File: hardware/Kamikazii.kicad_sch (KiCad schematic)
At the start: 36 parts, among them U1 L7805CV, U2 BP

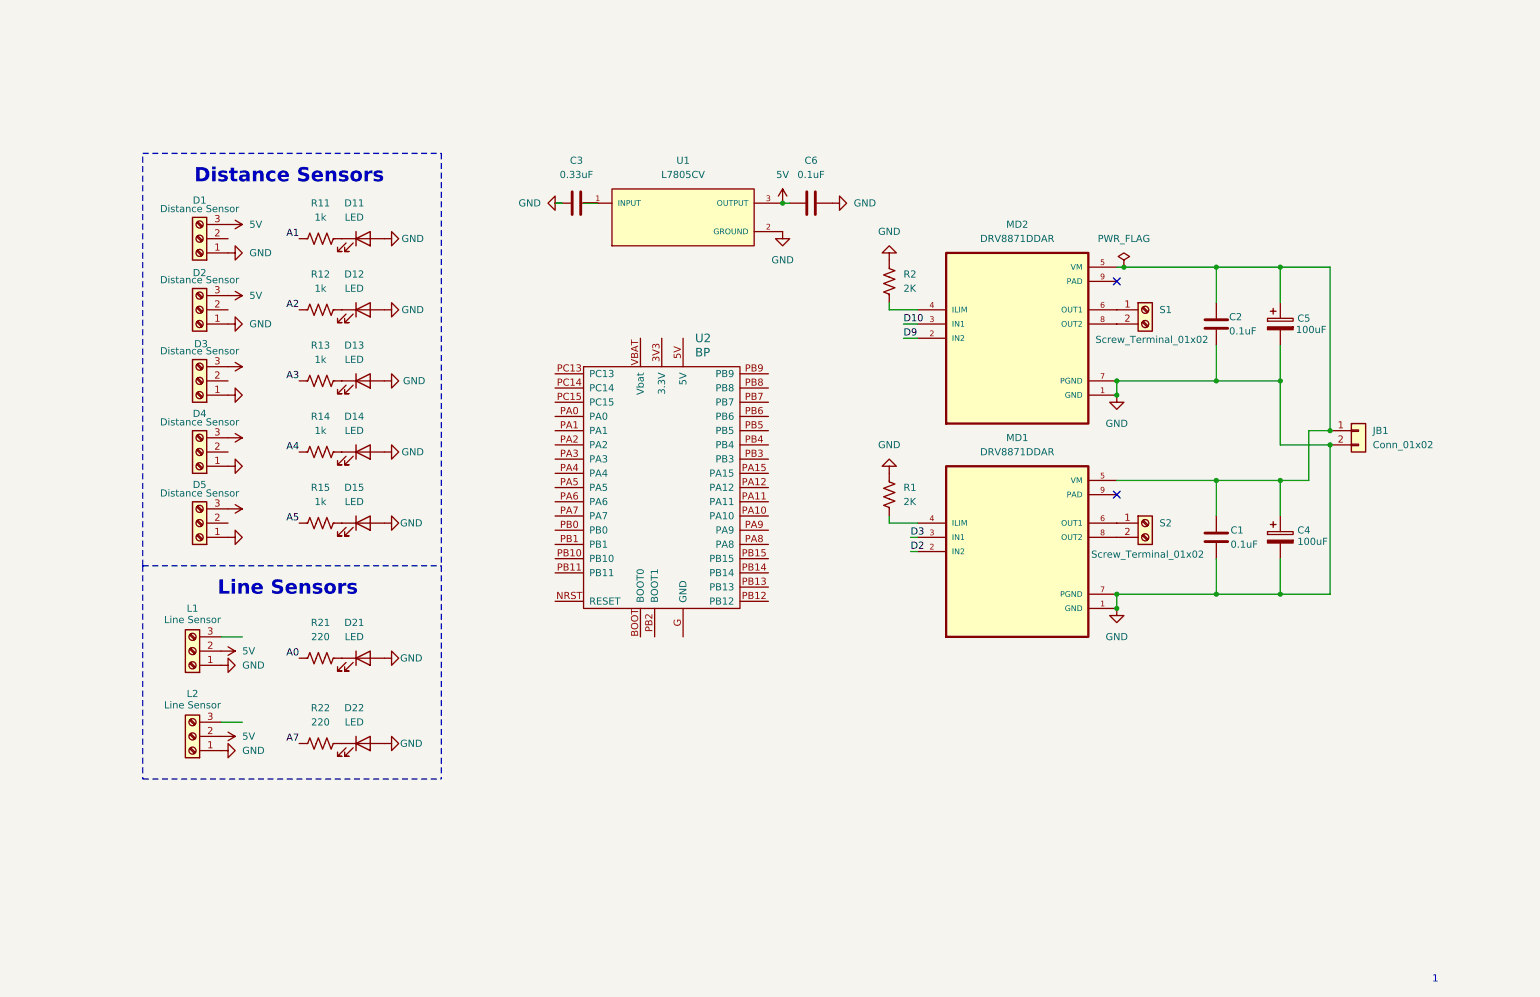
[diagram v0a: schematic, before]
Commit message: Add libraries for components
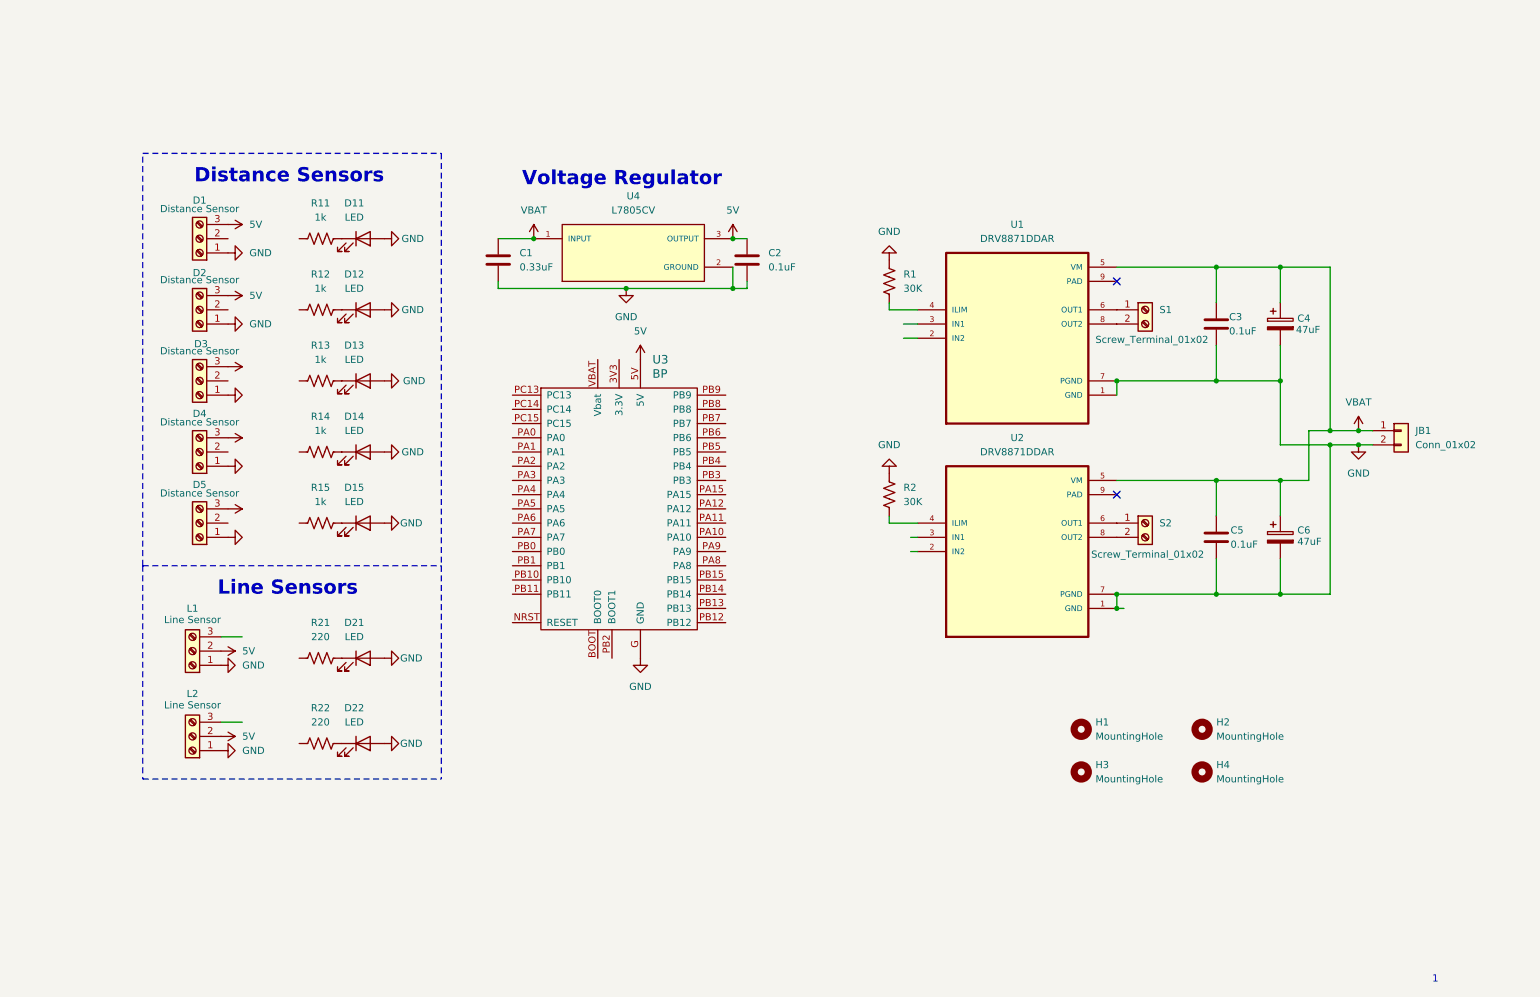
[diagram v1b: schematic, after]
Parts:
- removed MD1, MD2: DRV8871DDAR, DRV8871DDAR:VREG_LM5017MR_NOPB, symbol DRV8871DDAR:DRV8871DDAR
- removed U1: L7805CV, L7805CV:TO255P1040X460X1968-3, symbol L7805CV:L7805CV
- removed U2: BP, blue_pill:blue_pill, symbol STM32DB:BP
- added H1, H2, H3, H4: MountingHole, MountingHole:MountingHole_3.2mm_M3, symbol Mechanical:MountingHole
- added U1, U2: DRV8871DDAR, DRV8871DDAR:VREG_LM5017MR_NOPB, symbol DRV8871DDAR:DRV8871DDAR
- added U3: BP, blue_pill:blue_pill, symbol bp:BP
- added U4: L7805CV, L7805CV:TO255P1040X460X1968-3, symbol L7805CV:L7805CV
- C4: renamed from C5; value 100uF -> 47uF
- C6: renamed from C4; value 100uF -> 47uF
- R1: renamed from R2; value 2K -> 30K
- R2: renamed from R1; value 2K -> 30K
- renumbered C3 to C1, C6 to C2, C2 to C3, C1 to C5
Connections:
- net 5V: now also C2.2, U3.5V, U4.3 (OUTPUT); no longer C2.1
- net GND: now also C2.1, U1.1 (GND), U1.7 (PGND), U2.1 (GND), U2.7 (PGND), U3.G (GND), U4.2 (GROUND); no longer C2.2
- net VBAT: now reaches C3.1, C4.1, C5.1, C6.1, JB1.1 (Pin_1)
- net VBAT: now also C1.2, U1.5 (VM), U2.5 (VM), U4.1 (INPUT)
- net at S1.1 (Pin_1): now also U1.6 (OUT1)
- net at S1.2 (Pin_2): now also U1.8 (OUT2)
- net at R2.2: now also U2.4 (ILIM)
- net at S2.1 (Pin_1): now also U2.6 (OUT1)
- net at S2.2 (Pin_2): now also U2.8 (OUT2)
- net at R1.2: now also U1.4 (ILIM)
- net A0: no longer names the net of R21.1
- net A1: no longer names the net of R11.1
- net A2: no longer names the net of R12.1
- net A3: no longer names the net of R13.1
- net A4: no longer names the net of R14.1
- net A5: no longer names the net of R15.1
- net A7: no longer names the net of R22.1
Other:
- note added: "Voltage Regulator"
- moved on the sheet: C1, C2, JB1

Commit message: Finish schematic
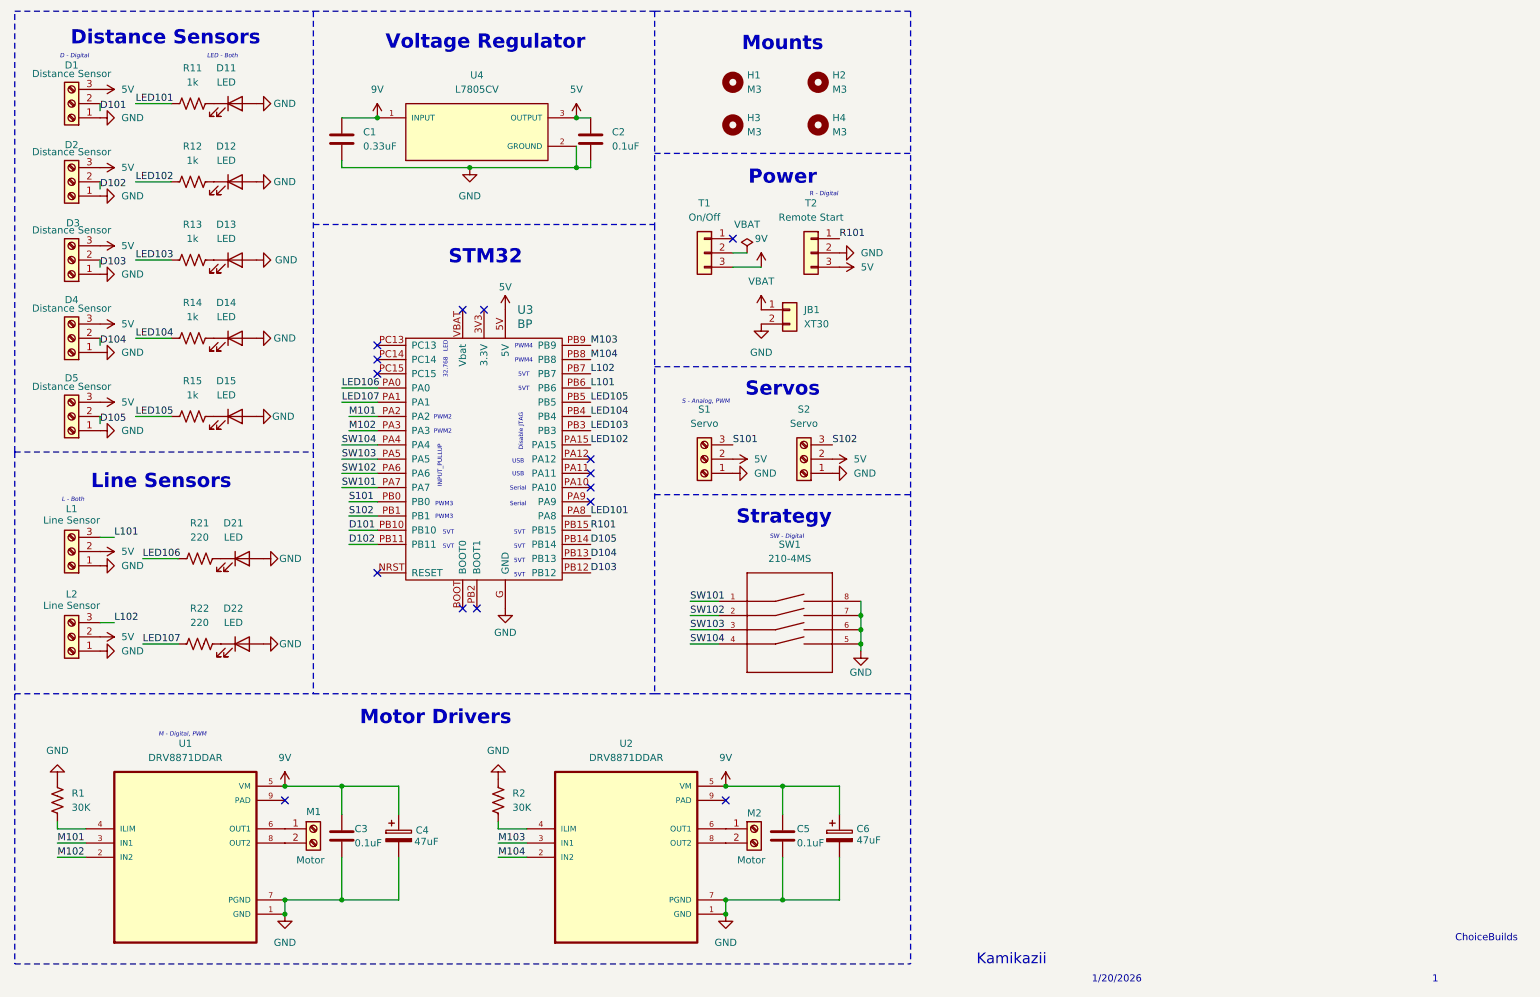
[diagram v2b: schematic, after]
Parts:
- added S1, S2: Servo, TerminalBlock:TerminalBlock_Xinya_XY308-2.54-2P_1x02_P2.54mm_Horizontal, symbol Connector:Screw_Terminal_01x03
- added SW1: 210-4MS, 210-4MS:DIP8_210-4_CTS, symbol 210-4MS:210-4MS
- added T1: On/Off, symbol Connector_Generic:Conn_01x03
- added T2: Remote Start, symbol Connector_Generic:Conn_01x03
- H1, H2, H3, H4: value MountingHole -> M3
- JB1: value Conn_01x02 -> XT30
- M1: renamed from S1; value Screw_Terminal_01x02 -> Motor
- M2: renamed from S2; value Screw_Terminal_01x02 -> Motor
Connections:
- net 5V: now also S1.2 (Pin_2), S2.2 (Pin_2), T2.3 (Pin_3)
- net GND: now also S1.1 (Pin_1), S2.1 (Pin_1), SW1.5, SW1.6, SW1.7, SW1.8, T2.2 (Pin_2)
- net VBAT: no longer C1.2, C3.1, C4.1, C5.1, C6.1, U1.5 (VM), U2.5 (VM), U4.1 (INPUT)
- net D102: now reaches D2.2 (Pin_2)
- net D102: now also U3.PB11
- net LED105: now reaches R15.1
- net LED105: now also U3.PB5
- net LED104: now reaches R14.1
- net LED104: now also U3.PB4
- net D101: now reaches D1.2 (Pin_2)
- net D101: now also U3.PB10
- net LED102: now reaches R12.1
- net LED102: now also U3.PA15
- net D105: now reaches D5.2 (Pin_2)
- net D105: now also U3.PB14
- net M104: now reaches U2.2 (IN2)
- net M104: now also U3.PB8
- net M103: now reaches U2.3 (IN1)
- net M103: now also U3.PB9
- net LED103: now reaches R13.1
- net LED103: now also U3.PB3
- net L101: now reaches L1.3 (Pin_3)
- net L101: now also U3.PB6
- net D103: now reaches D3.2 (Pin_2)
- net D103: now also U3.PB12
- net LED107: now reaches R22.1
- net LED107: now also U3.PA1
- net LED106: now reaches R21.1
- net LED106: now also U3.PA0
- net M102: now reaches U1.2 (IN2)
- net M102: now also U3.PA3
- net M101: now reaches U1.3 (IN1)
- net M101: now also U3.PA2
- net LED101: now reaches R11.1
- net LED101: now also U3.PA8
- net L102: now reaches L2.3 (Pin_3)
- net L102: now also U3.PB7
- net D104: now reaches D4.2 (Pin_2)
- net D104: now also U3.PB13
- net SW104: now reaches U3.PA4
- net SW104: now also SW1.4
- net SW103: now reaches U3.PA5
- net SW103: now also SW1.3
- net SW102: now reaches U3.PA6
- net SW102: now also SW1.2
- net SW101: now reaches U3.PA7
- net SW101: now also SW1.1
- net S101: now reaches U3.PB0
- net S101: now also S1.3 (Pin_3)
- net S102: now reaches U3.PB1
- net S102: now also S2.3 (Pin_3)
- net R101: now reaches U3.PB15
- net R101: now also T2.1 (Pin_1)
- new net 9V: C1.2, C3.1, C4.1, C5.1, C6.1, T1.3 (Pin_3), U1.5 (VM), U2.5 (VM), U4.1 (INPUT)
- no-connect marks 2 -> 15
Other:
- note added: "1/20/2026"
- note added: "32.768"
- note added: "5VT"
- note added: "ChoiceBuilds"
- note added: "D - Digital"
- note added: "Disable JTAG"
- note added: "INPUT_PULLUP"
- note added: "Kamikazii"
- note added: "L - Both"
- note added: "LED"
- note added: "LED - Both"
- note added: "M - Digital, PWM"
- note added: "Motor Drivers"
- note added: "Mounts"
- note added: "PWM2"
- note added: "PWM3"
- note added: "PWM4"
- note added: "Power"
- note added: "R - Digital"
- note added: "S - Analog, PWM"
- note added: "STM32"
- note added: "SW - Digital"
- note added: "Serial"
- note added: "Servos"
- note added: "Strategy"
- note added: "USB"
- moved on the sheet: C1, C2, C3, C4, C5, C6, D1, D11, D12, D13, D14, D15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

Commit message: Add more capacitors and pass ERC
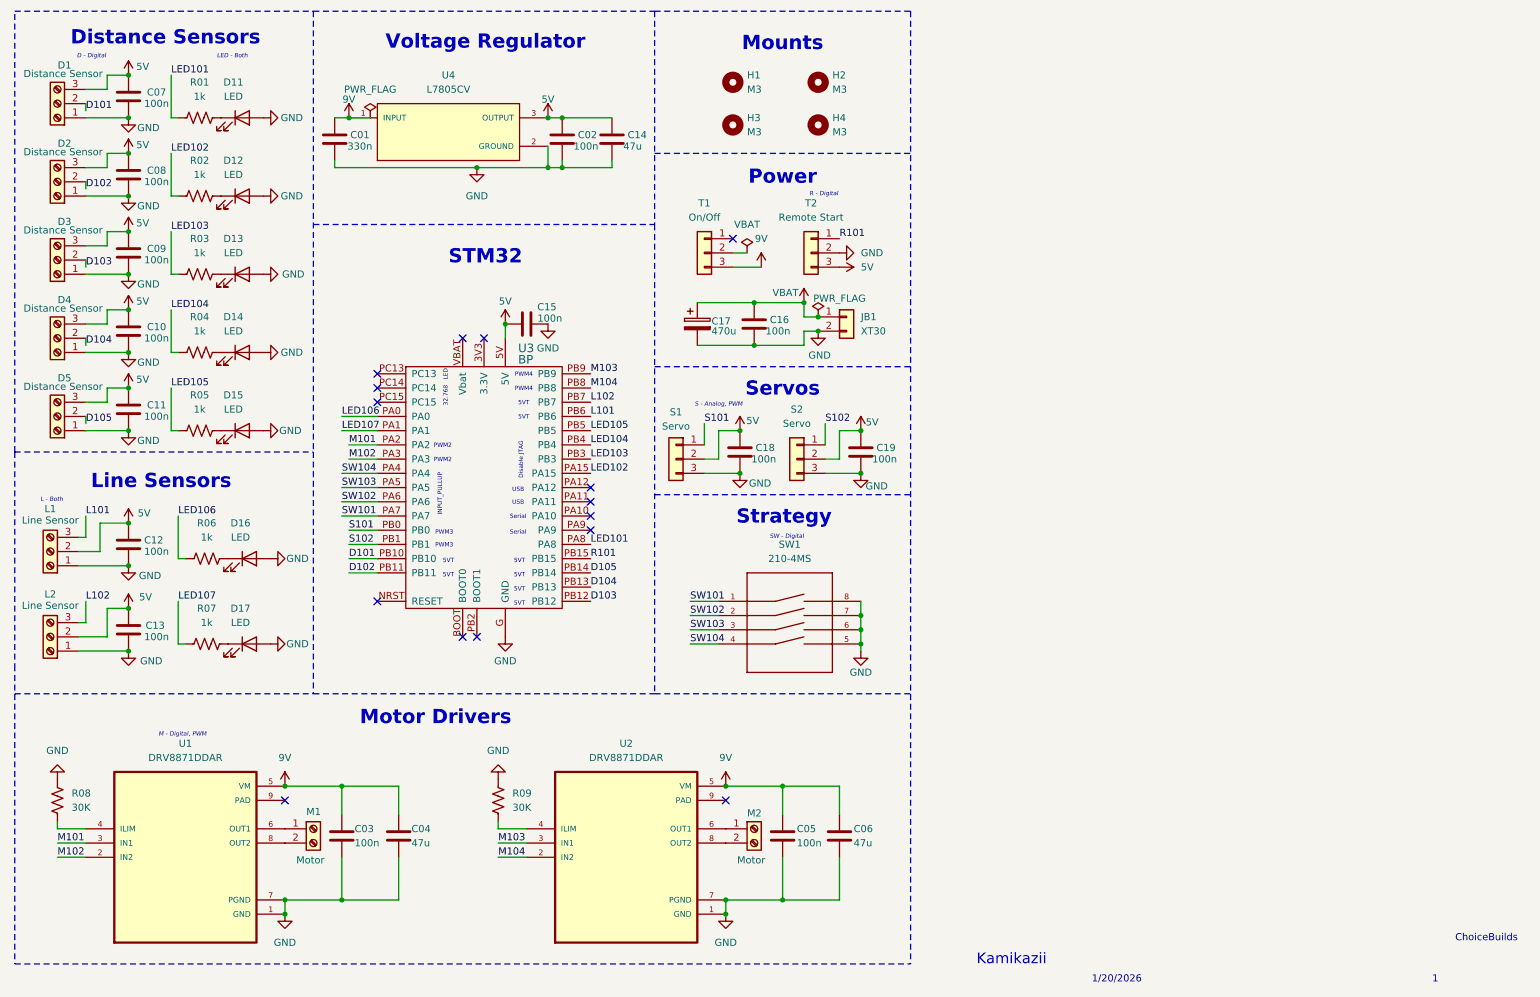
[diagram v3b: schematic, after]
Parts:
- removed C4, C6: 47uF, Capacitor_THT:C_Radial_D6.3mm_H11.0mm_P2.50mm, symbol Device:C_Polarized
- removed S1, S2: Servo, TerminalBlock:TerminalBlock_Xinya_XY308-2.54-2P_1x02_P2.54mm_Horizontal, symbol Connector:Screw_Terminal_01x03
- added C04, C06, C14: 47u, Capacitor_SMD:C_1210_3225Metric, symbol Device:C
- added C07, C08, C09, C10, C11, C12, C13, C15, C16, C18, C19: 100n, Capacitor_SMD:C_0402_1005Metric, symbol Device:C
- added C17: 470u, Capacitor_THT:CP_Radial_D8.0mm_P3.50mm, symbol Device:C_Polarized
- added S1, S2: Servo, Connector_PinHeader_2.54mm:PinHeader_1x03_P2.54mm_Vertical, symbol Connector_Generic:Conn_01x03
- C01: renamed from C1; value 0.33uF -> 330n; footprint Capacitor_THT:C_Disc_D3.0mm_W1.6mm_P2.50mm -> Capacitor_SMD:C_0402_1005Metric
- C02: renamed from C2; value 0.1uF -> 100n; footprint Capacitor_THT:C_Disc_D3.0mm_W1.6mm_P2.50mm -> Capacitor_SMD:C_0402_1005Metric
- C03: renamed from C3; value 0.1uF -> 100n; footprint Capacitor_THT:C_Disc_D3.0mm_W1.6mm_P2.50mm -> Capacitor_SMD:C_0402_1005Metric
- C05: renamed from C5; value 0.1uF -> 100n; footprint Capacitor_THT:C_Disc_D3.0mm_W1.6mm_P2.50mm -> Capacitor_SMD:C_0402_1005Metric
- D11, D12, D13, D14, D15: footprint LED_THT:LED_D5.0mm -> LED_SMD:LED_0402_1005Metric
- D16: renamed from D21; footprint LED_THT:LED_D5.0mm -> LED_SMD:LED_0402_1005Metric
- D17: renamed from D22; footprint LED_THT:LED_D5.0mm -> LED_SMD:LED_0402_1005Metric
- R01: renamed from R11; footprint Resistor_THT:R_Axial_DIN0207_L6.3mm_D2.5mm_P7.62mm_Horizontal -> Resistor_SMD:R_0402_1005Metric
- R02: renamed from R12; footprint Resistor_THT:R_Axial_DIN0207_L6.3mm_D2.5mm_P7.62mm_Horizontal -> Resistor_SMD:R_0402_1005Metric
- R03: renamed from R13; footprint Resistor_THT:R_Axial_DIN0207_L6.3mm_D2.5mm_P7.62mm_Horizontal -> Resistor_SMD:R_0402_1005Metric
- R04: renamed from R14; footprint Resistor_THT:R_Axial_DIN0207_L6.3mm_D2.5mm_P7.62mm_Horizontal -> Resistor_SMD:R_0402_1005Metric
- R05: renamed from R15; footprint Resistor_THT:R_Axial_DIN0207_L6.3mm_D2.5mm_P7.62mm_Horizontal -> Resistor_SMD:R_0402_1005Metric
- R06: renamed from R21; value 220 -> 1k; footprint Resistor_THT:R_Axial_DIN0207_L6.3mm_D2.5mm_P7.62mm_Horizontal -> Resistor_SMD:R_0402_1005Metric
- R07: renamed from R22; value 220 -> 1k; footprint Resistor_THT:R_Axial_DIN0207_L6.3mm_D2.5mm_P7.62mm_Horizontal -> Resistor_SMD:R_0402_1005Metric
- R08: renamed from R1; footprint Resistor_THT:R_Axial_DIN0207_L6.3mm_D2.5mm_P7.62mm_Horizontal -> Resistor_SMD:R_0402_1005Metric
- R09: renamed from R2; footprint Resistor_THT:R_Axial_DIN0207_L6.3mm_D2.5mm_P7.62mm_Horizontal -> Resistor_SMD:R_0402_1005Metric
- SW1: footprint 210-4MS:DIP8_210-4_CTS -> 210-4MS:210-4MS
- T1, T2: footprint (none) -> Connector_PinHeader_2.54mm:PinHeader_1x03_P2.54mm_Vertical
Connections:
- net 5V: now also C07.1, C08.1, C09.1, C10.1, C11.1, C12.1, C13.1, C14.2, C15.1, C18.2, C19.2, S1.2 (Pin_2), S2.2 (Pin_2)
- net 9V: now also C04.1, C06.1
- net GND: now also C04.2, C06.2, C07.2, C08.2, C09.2, C10.2, C11.2, C12.2, C13.2, C14.1, C15.2, C16.1, C17.2, C18.1, C19.1, S1.3 (Pin_3), S2.3 (Pin_3)
- net S101: now also S1.1 (Pin_1)
- net S102: now also S2.1 (Pin_1)
- net VBAT: now also C16.2, C17.1
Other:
- moved on the sheet: C01, C02, D1, D11, D12, D13, D14, D15, D16, D17, JB1, L1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
